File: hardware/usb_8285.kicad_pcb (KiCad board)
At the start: 2 copper layers, 20 parts, among them P1 UTX, P2 URX, P3 D+, P4 +5V, P5 +5V, P6 GND, P7 GND, P8 D-, P9 G0, U1 ESP8266EX, U2 MCP1824, X1 26MHz

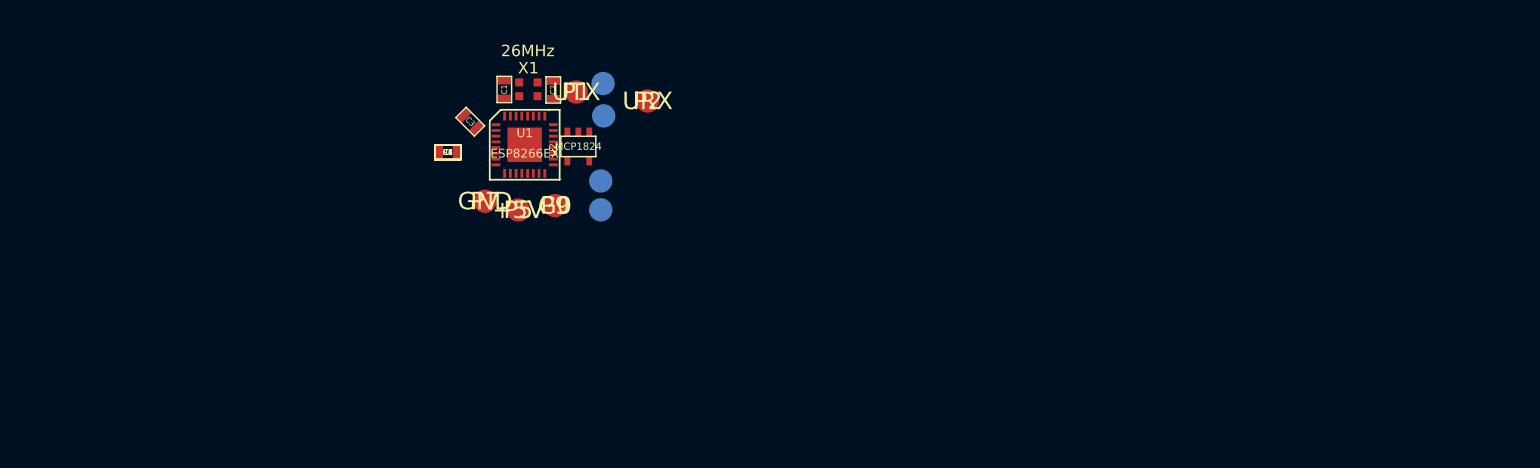
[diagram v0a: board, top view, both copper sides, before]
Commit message: Add Schematic updates.  Add a ton of comments in the ASM, optimize more for size, since speed on usb 1.1 low speed is sufficient.
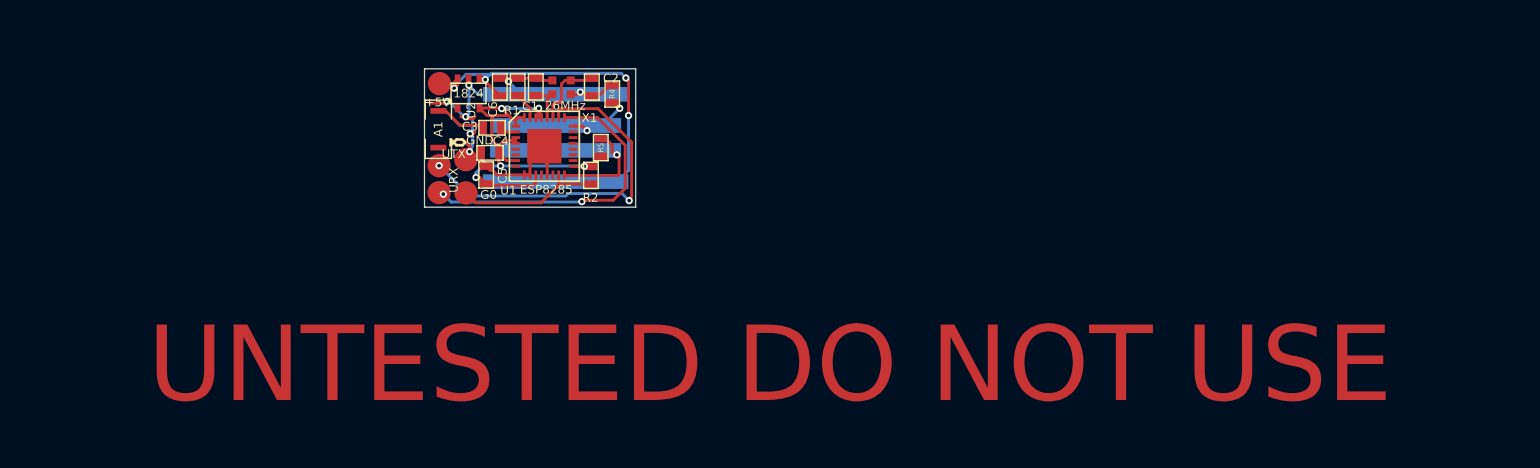
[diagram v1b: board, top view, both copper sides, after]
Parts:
- removed the P4 at (56.2, 27.1)
- added A1: ANT, SM1206, F.Cu at (41.8, 31.1)
- added P6: GND, .1SMTPIN, B.Cu at (52.1, 28.1)
- added R4: 1.5k, SM0603, F.Cu at (57.0, 28.0)
- added R5: 1.5k, SM0603, F.Cu at (56.0, 32.7)
- P4: renamed from P6; value GND -> +5V
- U1: value ESP8266EX -> ESP8285
- U2: value MCP1824 -> 1824
- moved P2 19.9 mm to (41.9, 36.6)
- moved P1 13.6 mm to (41.9, 34.3)
- moved P5 13.0 mm to (41.9, 27.1)
- moved R2 12.6 mm to (55.2, 35.1), turned to 270 degrees
- moved U2 10.6 mm to (44.5, 28.0)
- moved R1 8.34 mm to (48.8, 27.4), turned to 270 degrees
- moved P9 7.84 mm to (44.3, 36.7)
- moved C6 7.28 mm to (47.2, 27.4), turned to 270 degrees
- moved P8 4.76 mm to (52.1, 33.0)
- moved P4 4.64 mm to (52.1, 35.7)
- moved P3 4.22 mm to (52.1, 30.5)
- moved P7 3.99 mm to (44.2, 33.8)
- moved C5 3.89 mm to (46.0, 35.1), turned to 270 degrees
- moved C4 3.68 mm to (46.4, 33.2)
- moved C2 3.37 mm to (55.2, 27.4)
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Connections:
- net N-000001 renamed /D+
- net N-000002 renamed /D-
- C3 pad 1: (no net) -> N-0000010
- P4 pad 1: GND -> +5V
- U1 pad 10: (no net) -> GND
- U1 pad 9: (no net) -> GND
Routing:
- net GND: track 0.00 -> 73.9 mm, vias 0 -> 7
- net +3.3V: track 0.00 -> 42.5 mm, vias 0 -> 5
- net +5V: track 0.00 -> 36.5 mm, vias 0 -> 4
- net N-000006: track 0.00 -> 32.0 mm, vias 0 -> 2
- net N-000005: track 0.00 -> 27.3 mm, vias 0 -> 2
- net /D-: track 0.00 -> 14.5 mm, vias 0 -> 1
- net N-000003: track 0.00 -> 12.8 mm
- net /D+: track 0.00 -> 11.5 mm, vias 0 -> 2
- net N-0000026: track 0.00 -> 6.34 mm
- net N-0000010: track 0.00 -> 4.53 mm
- net N-0000025: track 0.00 -> 3.74 mm
- net N-0000015: track 0.00 -> 2.35 mm
- net N-0000019: track 0.00 -> 1.45 mm
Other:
- board outline added: 18.4 x 12.1 mm
- net class Default: clearance 0.254 -> 0.2413; via_dia 0.889 -> 0.635; via_drill 0.635 -> 0.3556
- rule trace_clearance: 0.254 -> 0.2413
- rule via_min_drill: 0.508 -> 0.3302
- rule via_min_size: 0.889 -> 0.6096
- board text added: "Rev -"
- board text added: "UNTESTED DO NOT USE"
- board text added: "usb_8285"

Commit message: update design to what I actually ordered
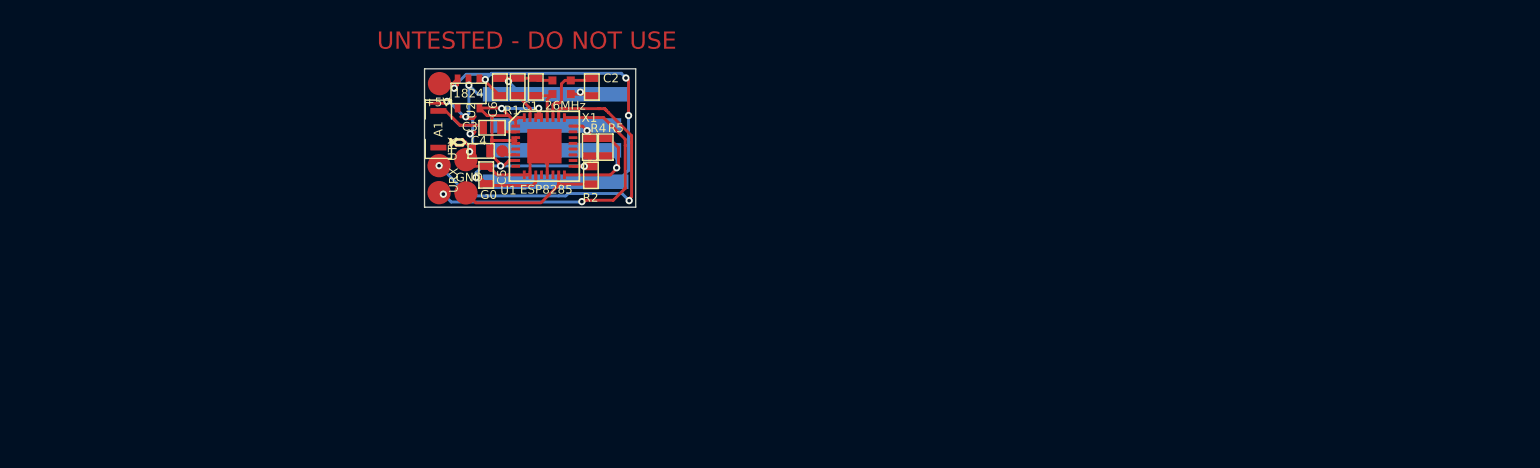
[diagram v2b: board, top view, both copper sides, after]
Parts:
- added P10: ADC, .1SMTPIN, F.Cu at (47.4, 33.0)
- moved R4 5.04 mm to (55.0, 32.7), turned to 270 degrees
- moved C4 0.80 mm to (45.6, 33.0)
- moved R5 0.43 mm to (56.4, 32.7)
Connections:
- R4 pad 2: GND -> +3.3V
- U1 pad 6: (no net) -> N-000007
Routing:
- net /D+: track 11.5 -> 5.09 mm, vias 2 -> 1
- net GND: track 73.9 -> 68.8 mm
- net N-000007: track 0.00 -> 1.30 mm
- net +3.3V: track 42.5 -> 43.4 mm
- net /D-: track 14.5 -> 15.2 mm
- net N-000005: track 32.0 -> 32.6 mm
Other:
- board text added: "UNTESTED - DO NOT USE"
- board text removed: "UNTESTED DO NOT USE"
